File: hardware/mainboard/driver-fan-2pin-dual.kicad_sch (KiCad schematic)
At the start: 11 parts, among them J12 JST XH, Q1 AGM308MBP, SW3 SPDT, 2A

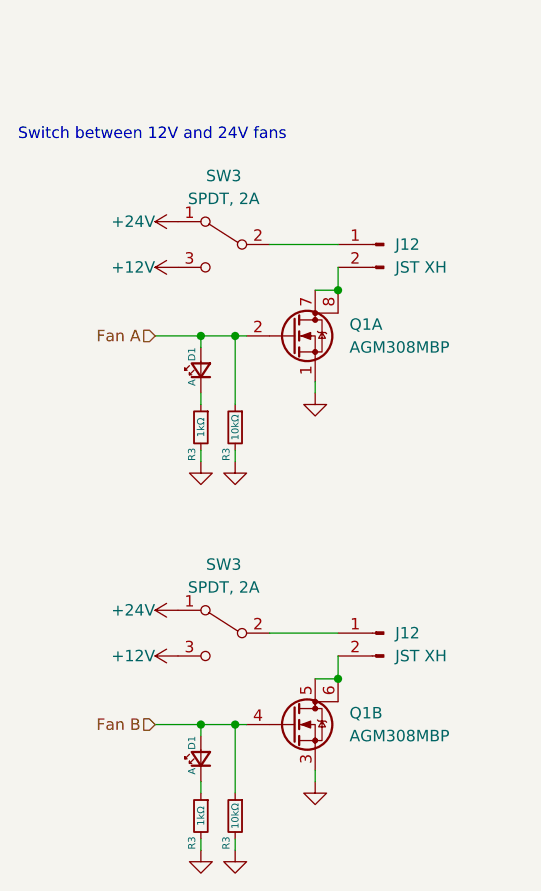
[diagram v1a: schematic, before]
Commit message: further board edits, mostly done with power planes, heaters, fans, motor channels, starting work on microcontroller signals
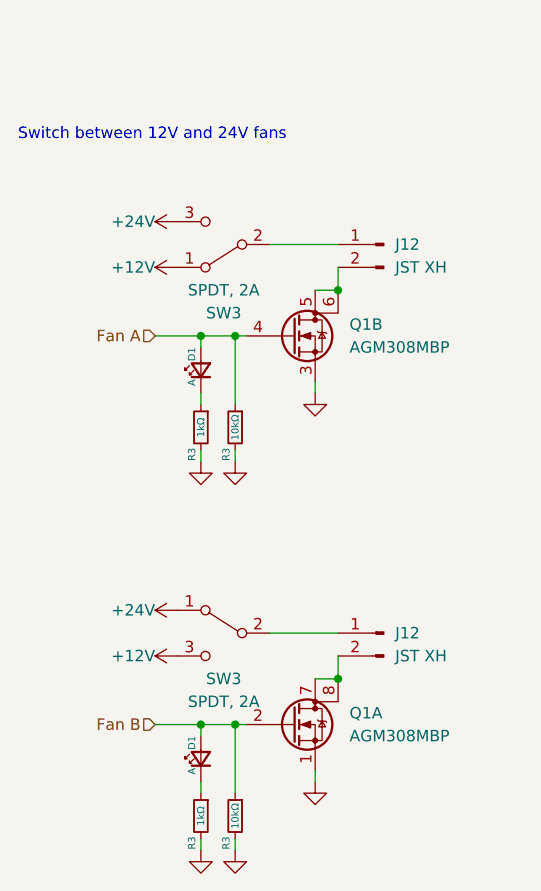
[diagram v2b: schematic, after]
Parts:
- R3: footprint AlphaLib:0603R -> AlphaLib:0402R
- SW3: footprint corevus:MS-22D28_SPST -> corevus:MS-22C01_SPDT
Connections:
- net +12V: now also SW3.1 (A); no longer SW3.3 (C)
- net +24V: now also SW3.3 (C); no longer SW3.1 (A)
- net Fan A: now also Q1.4 (G); no longer Q1.2 (G)
- net Fan B: now also Q1.2 (G); no longer Q1.4 (G)
- net at Q1.5 (D), Q1.6 (D): now also J12.2 (Pin_2); no longer J12.2 (Pin_2)
- net at Q1.7 (D), Q1.8 (D): now also J12.2 (Pin_2); no longer J12.2 (Pin_2)
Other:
- moved on the sheet: Q1A, Q1B, SW3
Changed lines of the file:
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@@
   (junction (at 67.31 99.06) (diameter 0) (color 0 0 0 0)
   )
+  (junction (at 82.55 93.98) (diameter 0) (color 0 0 0 0)
+  )
   (junction (at 71.12 55.88) (diameter 0) (color 0 0 0 0)
   )
+  (junction (at 71.12 99.06) (diameter 0) (color 0 0 0 0)
+  )
   (junction (at 82.55 50.8) (diameter 0) (color 0 0 0 0)
-  )
-  (junction (at 71.12 99.06) (diameter 0) (color 0 0 0 0)
-  )
-  (junction (at 82.55 93.98) (diameter 0) (color 0 0 0 0)
   )
   (wire (pts (xy 67.31 100.33) (xy 67.31 99.06))
@@
     (effects (font (size 1.27 1.27)) (justify right))
   )
-  (symbol (lib_id "Device:Q_Dual_NMOS_S1G1S2G2D2D2D1D1") (at 77.47 99.06 0) (unit 2)
+  (symbol (lib_id "Device:Q_Dual_NMOS_S1G1S2G2D2D2D1D1") (at 77.47 55.88 0) (unit 2)
     (in_bom yes) (on_board yes) (dnp no) (fields_autoplaced)
-    (property "Reference" "Q1" (at 83.82 97.79 0)
+    (property "Reference" "Q1" (at 83.82 54.61 0)
       (effects (font (size 1.27 1.27)) (justify left))
     )
-    (property "Value" "AGM308MBP" (at 83.82 100.33 0)
+    (property "Value" "AGM308MBP" (at 83.82 57.15 0)
       (effects (font (size 1.27 1.27)) (justify left))
     )
-    (property "Footprint" "corevus:AGM308MBP" (at 82.55 99.06 0)
-      (effects (font (size 1.27 1.27)) hide)
-    )
-    (property "Datasheet" "~" (at 82.55 99.06 0)
+    (property "Footprint" "corevus:AGM308MBP" (at 82.55 55.88 0)
+      (effects (font (size 1.27 1.27)) hide)
+    )
+    (property "Datasheet" "~" (at 82.55 55.88 0)
       (effects (font (size 1.27 1.27)) hide)
     )
@@
       (effects (font (size 0.8 0.8)))
     )
-    (property "Footprint" "AlphaLib:0603R" (at 71.12 66.04 0)
+    (property "Footprint" "AlphaLib:0402R" (at 71.12 66.04 0)
       (effects (font (size 1.27 1.27)) hide)
     )
@@
       (effects (font (size 0.8 0.8)))
     )
-    (property "Footprint" "AlphaLib:0603R" (at 71.12 109.22 0)
+    (property "Footprint" "AlphaLib:0402R" (at 71.12 109.22 0)
       (effects (font (size 1.27 1.27)) hide)
     )
@@
     )
   )
-  (symbol (lib_id "Switch:SW_SPDT") (at 69.85 45.72 0) (mirror y) (unit 1)
-    (in_bom yes) (on_board yes) (dnp no) (fields_autoplaced)
-    (property "Reference" "SW3" (at 69.85 38.1 0)
+  (symbol (lib_id "Switch:SW_SPDT") (at 69.85 45.72 180) (unit 1)
+    (in_bom yes) (on_board yes) (dnp no)
+    (property "Reference" "SW3" (at 69.85 53.34 0)
       (effects (font (size 1.27 1.27)))
     )
-    (property "Value" "SPDT, 2A" (at 69.85 40.64 0)
+    (property "Value" "SPDT, 2A" (at 69.85 50.8 0)
       (effects (font (size 1.27 1.27)))
     )
-    (property "Footprint" "corevus:MS-22D28_SPST" (at 69.85 45.72 0)
+    (property "Footprint" "corevus:MS-22C01_SPDT" (at 69.85 45.72 0)
       (effects (font (size 1.27 1.27)) hide)
     )
@@
   )
   (symbol (lib_id "Switch:SW_SPDT") (at 69.85 88.9 0) (mirror y) (unit 1)
-    (in_bom yes) (on_board yes) (dnp no) (fields_autoplaced)
-    (property "Reference" "SW3" (at 69.85 81.28 0)
+    (in_bom yes) (on_board yes) (dnp no)
+    (property "Reference" "SW3" (at 69.85 93.98 0)
       (effects (font (size 1.27 1.27)))
     )
-    (property "Value" "SPDT, 2A" (at 69.85 83.82 0)
+    (property "Value" "SPDT, 2A" (at 69.85 96.52 0)
       (effects (font (size 1.27 1.27)))
     )
-    (property "Footprint" "corevus:MS-22D28_SPST" (at 69.85 88.9 0)
+    (property "Footprint" "corevus:MS-22C01_SPDT" (at 69.85 88.9 0)
       (effects (font (size 1.27 1.27)) hide)
     )
@@
       (effects (font (size 0.8 0.8)))
     )
-    (property "Footprint" "AlphaLib:0603R" (at 67.31 109.22 0)
+    (property "Footprint" "AlphaLib:0402R" (at 67.31 109.22 0)
       (effects (font (size 1.27 1.27)) hide)
     )
@@
     )
   )
-  (symbol (lib_id "Device:Q_Dual_NMOS_S1G1S2G2D2D2D1D1") (at 77.47 55.88 0) (unit 1)
+  (symbol (lib_id "Device:Q_Dual_NMOS_S1G1S2G2D2D2D1D1") (at 77.47 99.06 0) (unit 1)
     (in_bom yes) (on_board yes) (dnp no) (fields_autoplaced)
-    (property "Reference" "Q1" (at 83.82 54.61 0)
+    (property "Reference" "Q1" (at 83.82 97.79 0)
       (effects (font (size 1.27 1.27)) (justify left))
     )
-    (property "Value" "AGM308MBP" (at 83.82 57.15 0)
+    (property "Value" "AGM308MBP" (at 83.82 100.33 0)
       (effects (font (size 1.27 1.27)) (justify left))
     )
-    (property "Footprint" "corevus:AGM308MBP" (at 82.55 55.88 0)
-      (effects (font (size 1.27 1.27)) hide)
-    )
-    (property "Datasheet" "~" (at 82.55 55.88 0)
+    (property "Footprint" "corevus:AGM308MBP" (at 82.55 99.06 0)
+      (effects (font (size 1.27 1.27)) hide)
+    )
+    (property "Datasheet" "~" (at 82.55 99.06 0)
       (effects (font (size 1.27 1.27)) hide)
     )
@@
       (effects (font (size 0.8 0.8)))
     )
-    (property "Footprint" "AlphaLib:0603R" (at 67.31 66.04 0)
-      (effects (font (size 1.27 1.27)) hide)
-    )
+    (property "Footprint" "AlphaLib:0402R" (at 67.31 66.04 0)
+      (effects (font (size 1.27 1.27)) hide)
+    )

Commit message: redoing board for version alpha 0.2
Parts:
- removed D1 (x2): A, AlphaLib:0603LED, symbol Device:LED_Small
- added D1 (x2): Red, AlphaLib:0402LED, symbol Device:LED_Small
- J12: footprint Connector_JST:JST_XH_B2B-XH-A_1x02_P2.50mm_Vertical -> corevus:ShouHan_2.54-2PLT
- renumbered Q1 to Q21
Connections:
- net Fan A: now also D1.2 (A)
- net Fan B: now also D1.2 (A)
- net at R3.1: now also D1.1 (K) (x2)

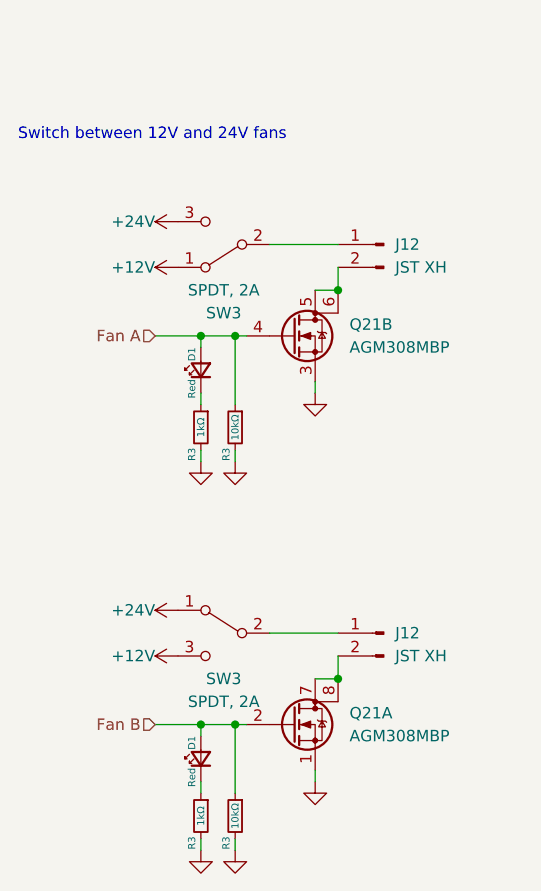
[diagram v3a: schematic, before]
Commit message: tested SMD style XH connectors — didn't work very well alas
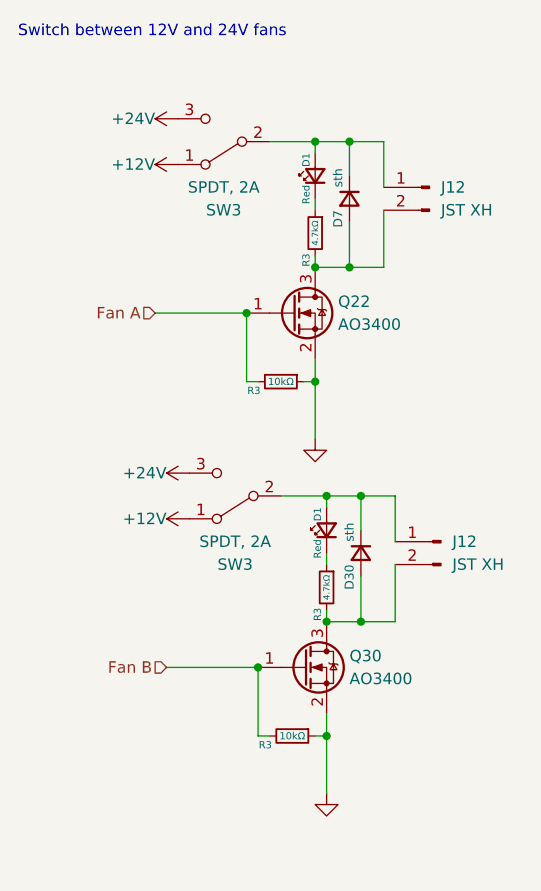
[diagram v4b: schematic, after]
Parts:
- removed D1 (x2): Red, AlphaLib:0402LED, symbol Device:LED_Small
- removed Q21: AGM308MBP, corevus:AGM308MBP, symbol Device:Q_Dual_NMOS_S1G1S2G2D2D2D1D1
- removed R3: 10kΩ, AlphaLib:0402R, symbol Device:R_Small
- removed R3 (x2): 1kΩ, AlphaLib:0402R, symbol Device:R_Small
- added D1 (x2): Red, AlphaLib:0402LED, symbol Device:LED_Small
- added D30, D7: sth, symbol Device:D_Small
- added Q22, Q30: AO3400, Package_TO_SOT_SMD:SOT-23, symbol Device:Q_NMOS_GSD
- added R3: 10kΩ, AlphaLib:0402R, symbol Device:R_Small
- added R3 (x2): 4.7kΩ, AlphaLib:0402R, symbol Device:R_Small
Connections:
- net +12V: now also SW3.1 (A); no longer SW3.3 (C)
- net +24V: now also SW3.3 (C); no longer SW3.1 (A)
- net Fan A: now also R3.2, Q22.1 (G); no longer R3.1
- net Fan B: now also Q30.1 (G), R3.2
- net GND: now also R3.1, Q22.2 (S), Q30.2 (S), R3.1; no longer R3.2
- net at J12.2 (Pin_2): now also D7.2 (A), Q22.3 (D), R3.2
- net at J12.1 (Pin_1), SW3.2 (B): now also D1.2 (A), D30.1 (K)
- net at J12.2 (Pin_2): now also D30.2 (A), Q30.3 (D), R3.2
- net at J12.1 (Pin_1), SW3.2 (B): now also D1.2 (A), D7.1 (K)
- new net: D1.1 (K), R3.1 (x2)
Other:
- moved on the sheet: J12, R3, SW3
